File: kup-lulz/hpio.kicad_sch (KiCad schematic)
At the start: 69 parts, among them J10 SFP_CAGE, J11 CONN_SFP_HOST, J12 SFP_CAGE, J33 CONN_SFP_HOST, J34 SFP_CAGE, J7 CONN_SFP_HOST, J8 SFP_CAGE, J9 CONN_SFP_HOST, U9 XILINX_ULTRASCALEPLUS_B676

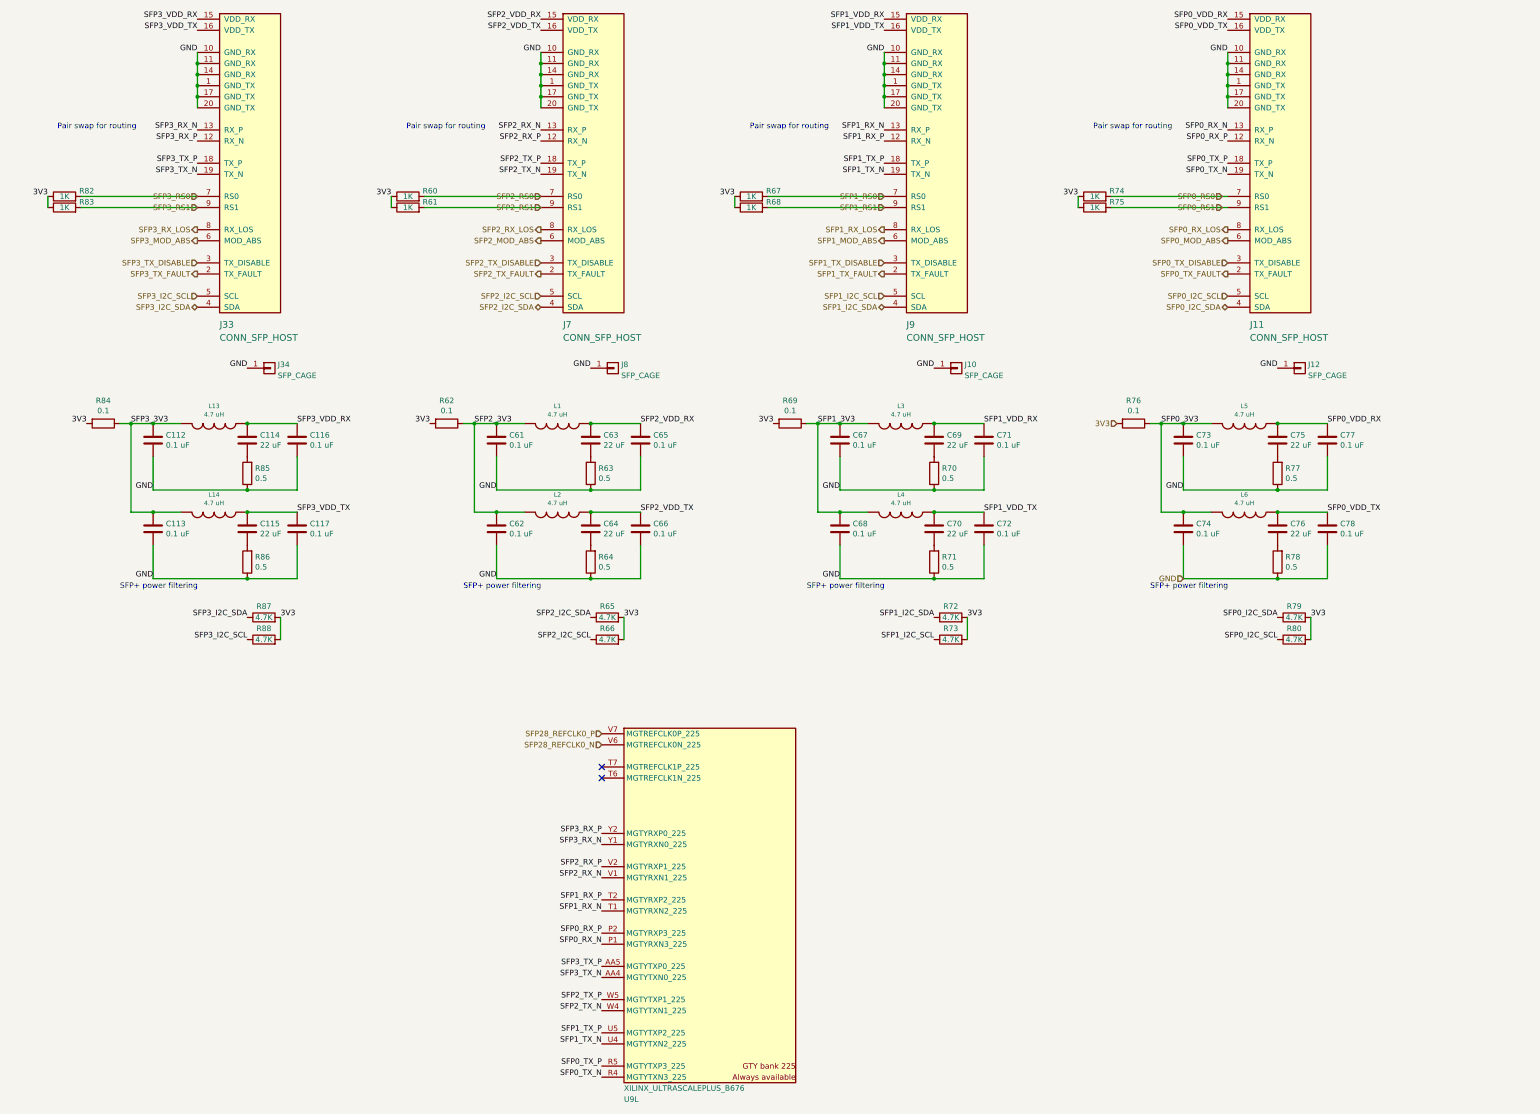
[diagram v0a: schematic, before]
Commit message: Continued initial layout of kup-lulz
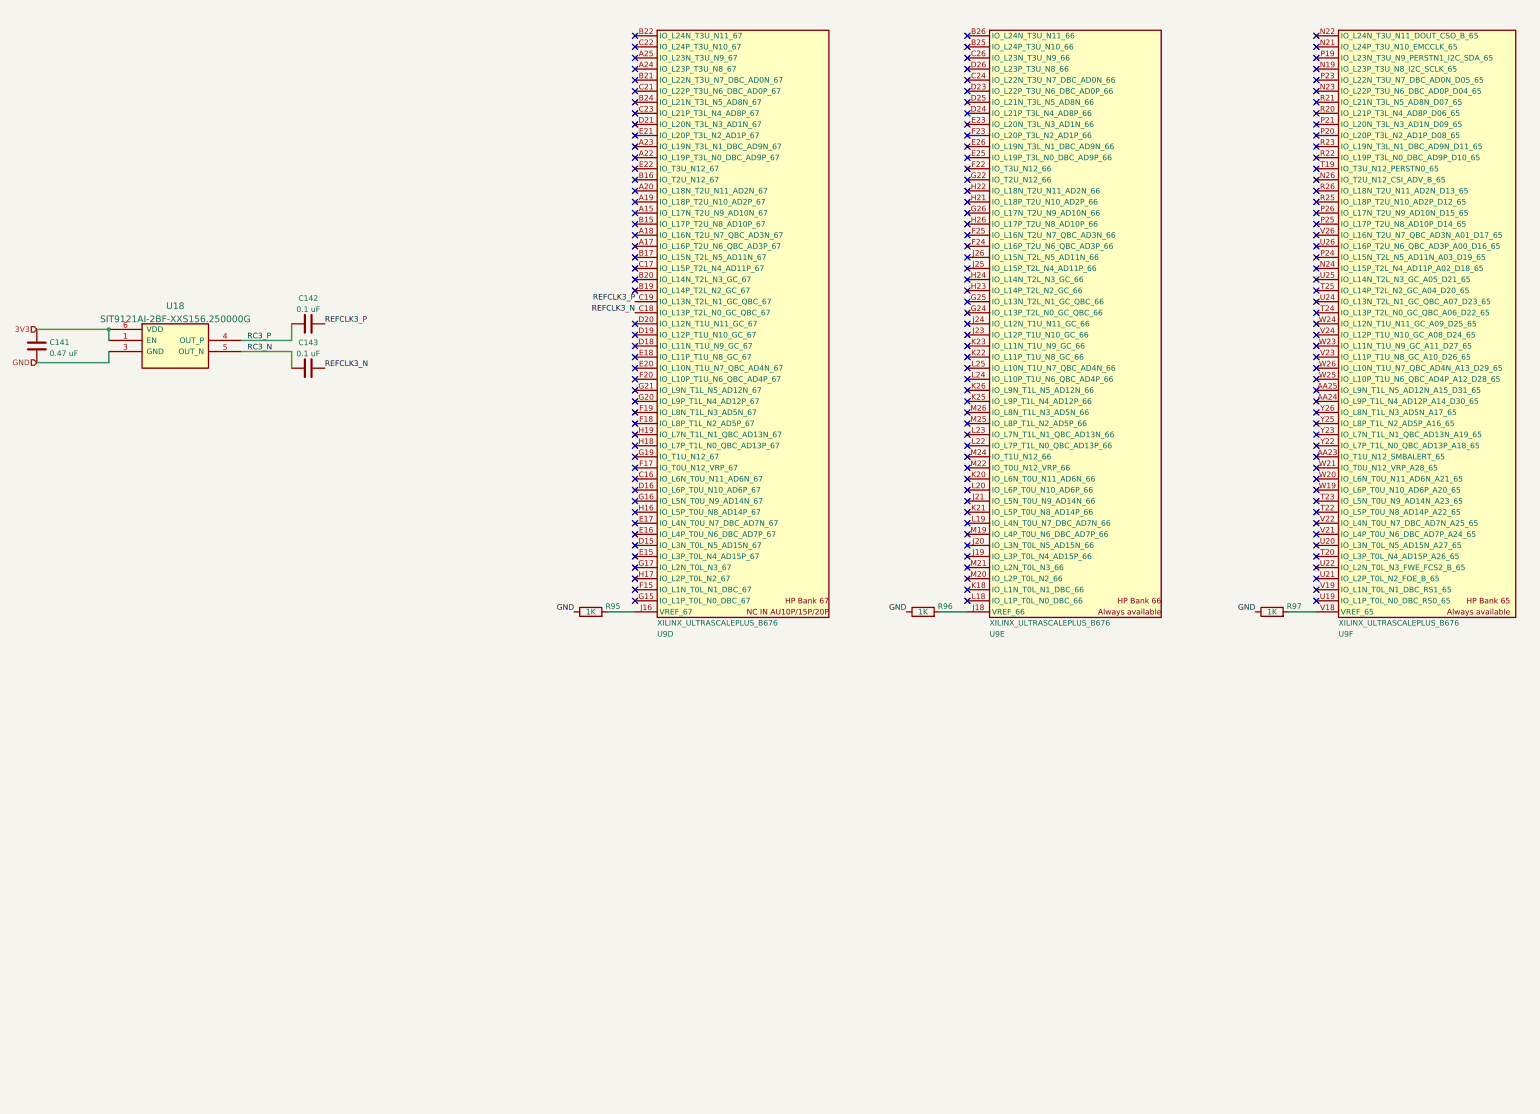
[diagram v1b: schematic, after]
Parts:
- removed C112, C113, C116, C117, C61, C62, C65, C66, C67, C68, C71, C72, C73, C74, C77, C78: 0.1 uF, azonenberg_pcb:EIA_0402_CAP_NOSILK, symbol device:C
- removed C114, C115, C63, C64, C69, C70, C75, C76: 22 uF, azonenberg_pcb:EIA_0805_CAP_NOSILK, symbol device:C
- removed J10, J12, J34, J8: SFP_CAGE, azonenberg_pcb:CONN_SFP_CAGE_TE_2007194-1, symbol conn:CONN_01X01
- removed J11, J33, J7, J9: CONN_SFP_HOST, azonenberg_pcb:CONN_SFP+_AMPHENOL_UE76_A10_2000T, symbol special-azonenberg:CONN_SFP_HOST
- removed L1, L13, L14, L2, L3, L4, L5, L6: 4.7 uH, azonenberg_pcb:EIA_0805_INDUCTOR_NOSILK, symbol passive-azonenberg:INDUCTOR_PWROUT
- removed R60, R61, R67, R68, R74, R75, R82, R83: 1K, azonenberg_pcb:EIA_0402_RES_NOSILK, symbol device:R
- removed R62, R69, R76, R84: 0.1, azonenberg_pcb:EIA_0402_RES_NOSILK, symbol device:R
- removed R63, R64, R70, R71, R77, R78, R85, R86: 0.5, azonenberg_pcb:EIA_0402_RES_NOSILK, symbol device:R
- removed R65, R66, R72, R73, R79, R80, R87, R88: 4.7K, azonenberg_pcb:EIA_0402_RES_NOSILK, symbol device:R
- removed U9: XILINX_ULTRASCALEPLUS_B676, azonenberg_pcb:BGA_676_27x27_FULLARRAY_1MM_FFG676, symbol xilinx-azonenberg:XILINX_ULTRASCALEPLUS_B676
- added C141: 0.47 uF, azonenberg_pcb:EIA_0402_CAP_NOSILK, symbol device:C
- added C142, C143: 0.1 uF, azonenberg_pcb:EIA_0402_CAP_NOSILK, symbol device:C
- added R95, R96, R97: 1K, azonenberg_pcb:EIA_0402_RES_NOSILK, symbol device:R
- added U18: SIT9121AI-2BF-XXS156.250000G, azonenberg_pcb:OSCILLATOR_LVDS_3.2x2.5, symbol osc-azonenberg:OSC_LVDS_NOPAD
- added U9: XILINX_ULTRASCALEPLUS_B676, azonenberg_pcb:BGA_676_27x27_FULLARRAY_1MM_FFG676, symbol xilinx-azonenberg:XILINX_ULTRASCALEPLUS_B676
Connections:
- net 3V3: now also C141.1, U18.1 (EN), U18.6 (VDD)
- net GND: now also C141.2, R95.1, R96.1, R97.1, U18.3 (GND)
- new net: R97.2, U9.V18 (VREF_65)
- new net: R95.2, U9.J16 (VREF_67)
- new net: R96.2, U9.J18 (VREF_66)
- new net RC3_N: C143.1, U18.5 (OUT_N)
- new net RC3_P: C142.1, U18.4 (OUT_P)
- new net REFCLK3_N: C143.2, U9.C18 (IO_L13P_T2L_N0_GC_QBC_67)
- new net REFCLK3_P: C142.2, U9.C19 (IO_L13N_T2L_N1_GC_QBC_67)
- no-connect marks 2 -> 154
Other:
- note removed: "Pair swap for routing"
- note removed: "SFP+ power filtering"

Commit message: Continued initial layout
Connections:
- net REFCLK3_N: now also U9.C19 (IO_L13N_T2L_N1_GC_QBC_67); no longer U9.C18 (IO_L13P_T2L_N0_GC_QBC_67)
- net REFCLK3_P: now also U9.C18 (IO_L13P_T2L_N0_GC_QBC_67); no longer U9.C19 (IO_L13N_T2L_N1_GC_QBC_67)
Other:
- note added: "Polarity invert for routing Nobody cares, just a 180 deg phase shift"
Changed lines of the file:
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@@
     (stroke (width 0) (type default) (color 0 0 0 0))
+  )
+  (text "Polarity invert for routing\nNobody cares, just a 180 deg phase shift"
+    (at 204.47 99.06 180)
+    (effects (font (size 1.27 1.27)) (justify right bottom))
   )
   (label "REFCLK3_N" (at 144.78 111.76 0)
     (effects (font (size 1.27 1.27)) (justify left bottom))
   )
-  (label "REFCLK3_N" (at 215.9 99.06 180)
+  (label "REFCLK3_N" (at 215.9 96.52 180)
     (effects (font (size 1.27 1.27)) (justify right bottom))
   )
@@
     (effects (font (size 1.27 1.27)) (justify left bottom))
   )
-  (label "REFCLK3_P" (at 215.9 96.52 180)
+  (label "REFCLK3_P" (at 215.9 99.06 180)
     (effects (font (size 1.27 1.27)) (justify right bottom))
   )

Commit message: Converted to kicad8 format, updated footprints and 3D models appropriately
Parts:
- added J14, J40: SMPM, azonenberg_pcb:CONN_SMPM_AMPHENOL_C925-197J-51PT, symbol conn:CONN_COAXIAL
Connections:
- net GND: now also J14.2 (Ext), J40.2 (Ext)
- net HPIO1_N: now reaches U9.A24 (IO_L23P_T3U_N8_67)
- net HPIO1_N: now also J40.1 (In)
- net HPIO1_P: now reaches U9.A25 (IO_L23N_T3U_N9_67)
- net HPIO1_P: now also J14.1 (In)
- no-connect marks 154 -> 152
